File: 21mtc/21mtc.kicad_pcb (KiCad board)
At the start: 2 copper layers, 48 x 24 mm, 6 parts, among them P101 CONN_01X06, P102 CONN_02X11, P103 CONN_01X11, P104 CONN_02X04, P105 CONN_01X04

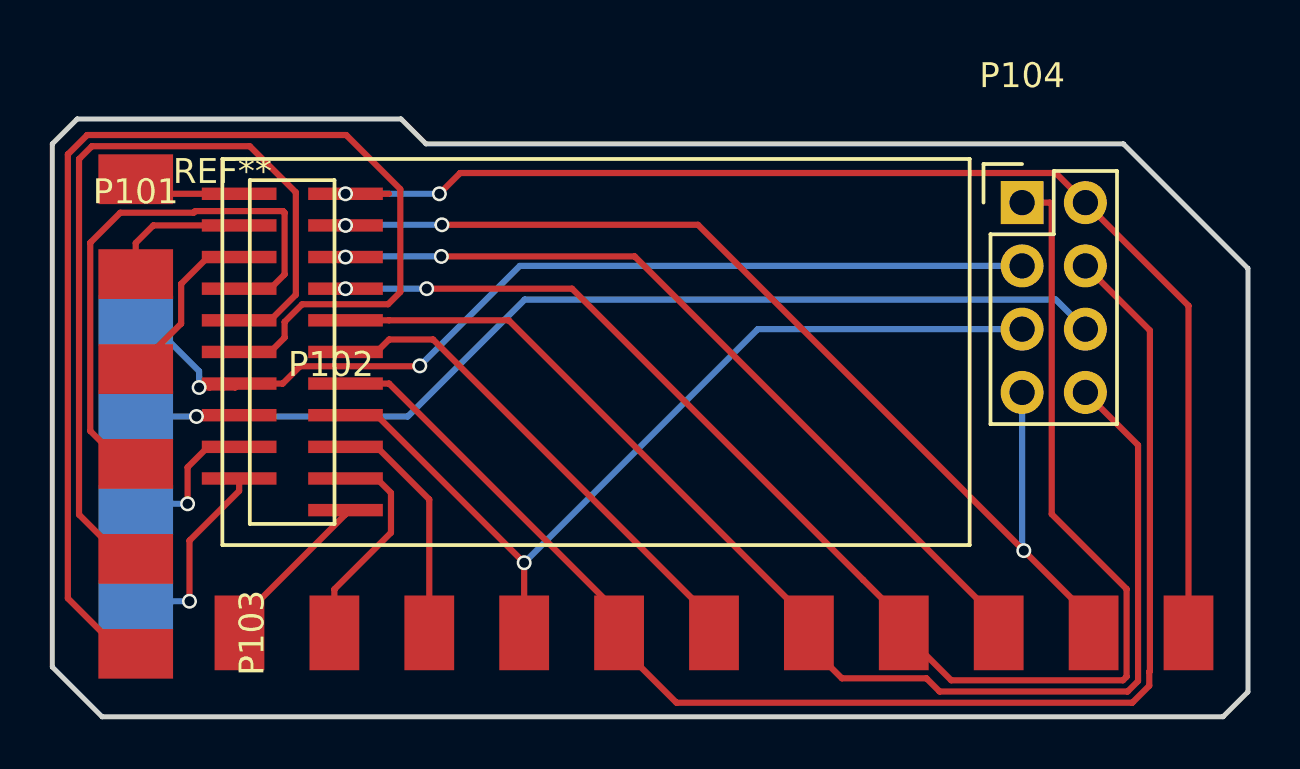
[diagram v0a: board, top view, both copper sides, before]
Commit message: Silkscreen and track width fixes
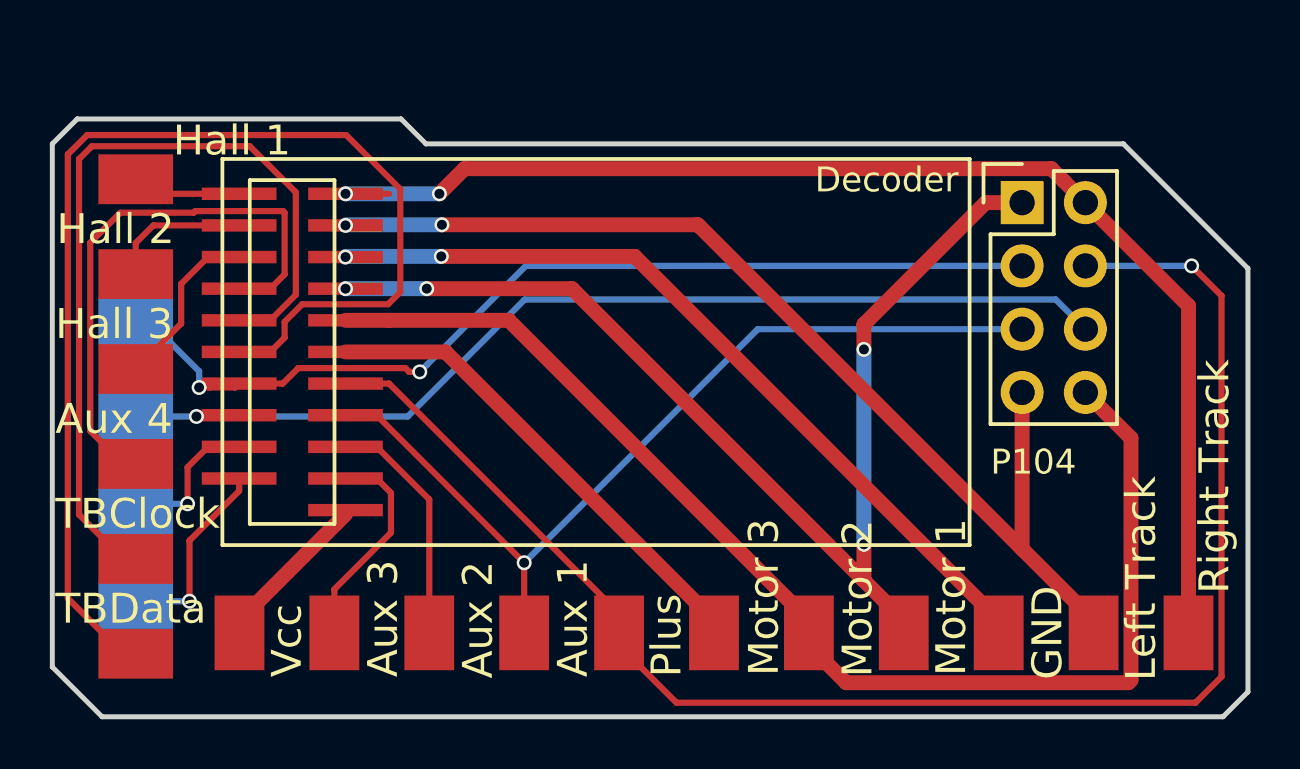
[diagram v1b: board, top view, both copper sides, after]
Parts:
- renumbered REF** to Decoder
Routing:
- net /Motor1: track 59.6 -> 47.1 mm, vias 2 -> 4
- net /Plus: track 56.5 -> 62.9 mm, vias 0 -> 1
- net /Motor3: track 20.2 -> 21.0 mm
- net /Motor2: track 51.2 -> 50.5 mm
- net /TrackL: vias 3 -> 2
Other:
- net class Power added: clearance 0.2, trace_width 0.6, via_dia 0.6, via_drill 0.4
- board text added: "Aux 1"
- board text added: "Aux 2"
- board text added: "Aux 3"
- board text added: "Aux 4"
- board text added: "GND"
- board text added: "Hall 1"
- board text added: "Hall 2"
- board text added: "Hall 3"
- board text added: "Left Track"
- board text added: "Motor 1"
- board text added: "Motor 2"
- board text added: "Motor 3"
- board text added: "Plus"
- board text added: "Right Track"
- board text added: "TBClock"
- board text added: "TBData"
- board text added: "Vcc"
